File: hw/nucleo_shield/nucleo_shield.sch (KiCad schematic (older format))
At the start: 36 parts, among them CN101 Nucleo-F411RE-CN10, CN71 Nucleo-F411RE-CN7, P1 CONN_01X10, P2 CONN_01X10, P3 CONN_01X10, P4 CONN_01X02, P5 CONN_01X06, U1 74HC595, U2 74HC595, U3 LTV-847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

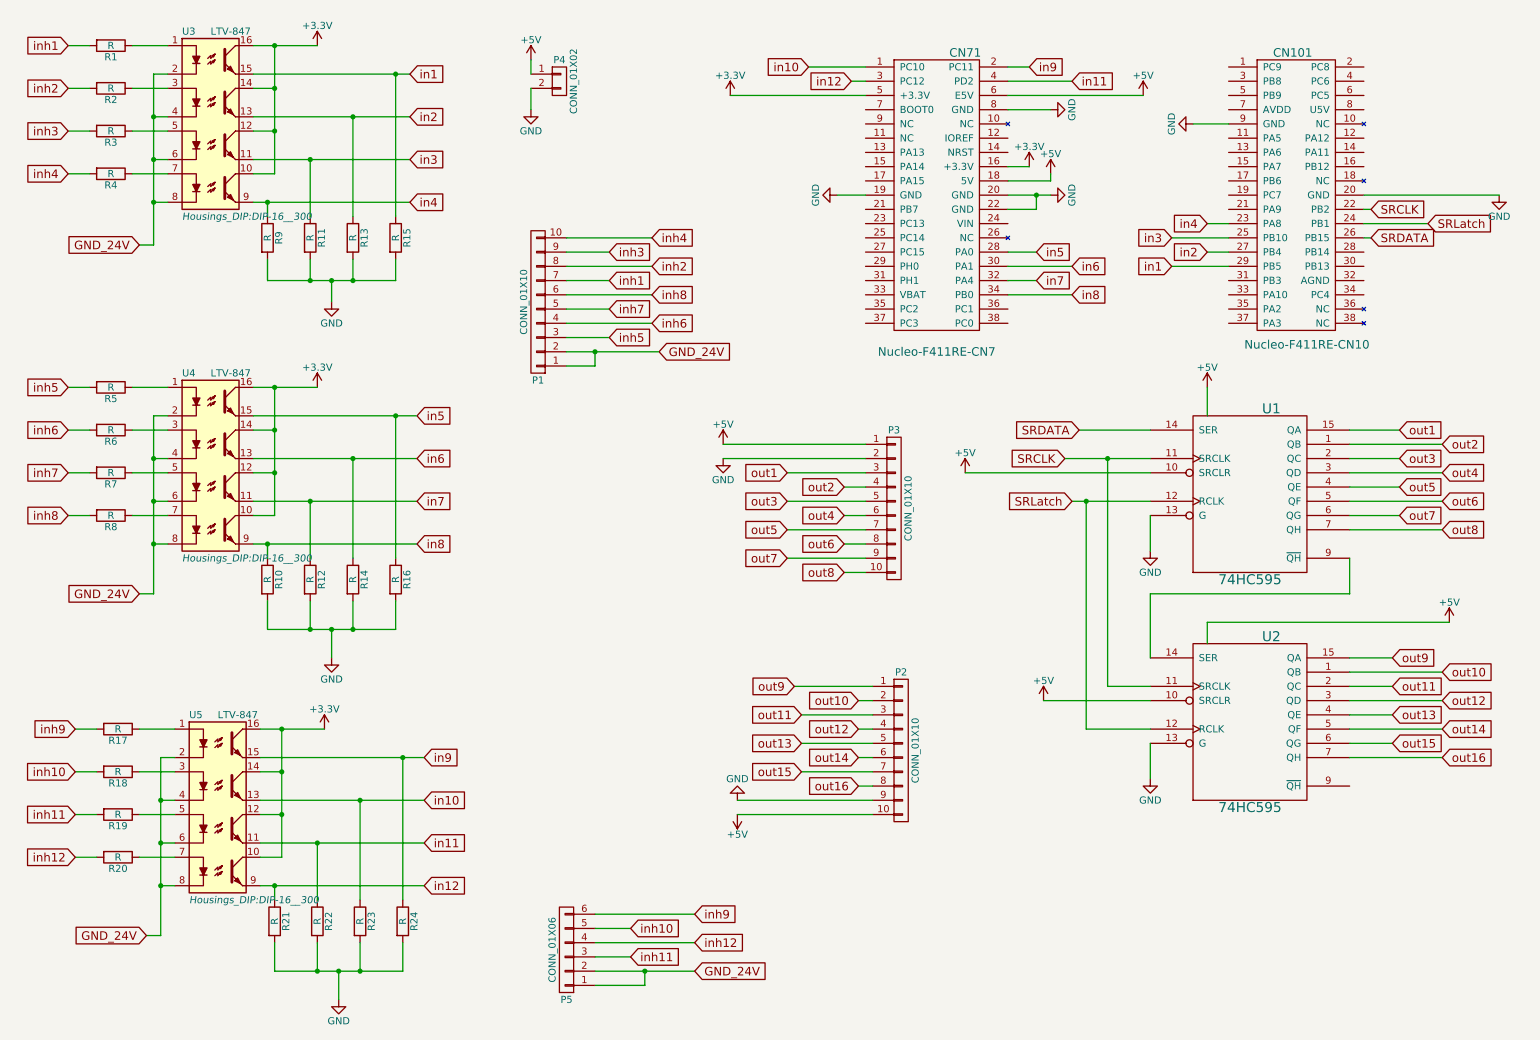
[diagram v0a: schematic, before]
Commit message: HW: modify nucleo with hierarchical sheets
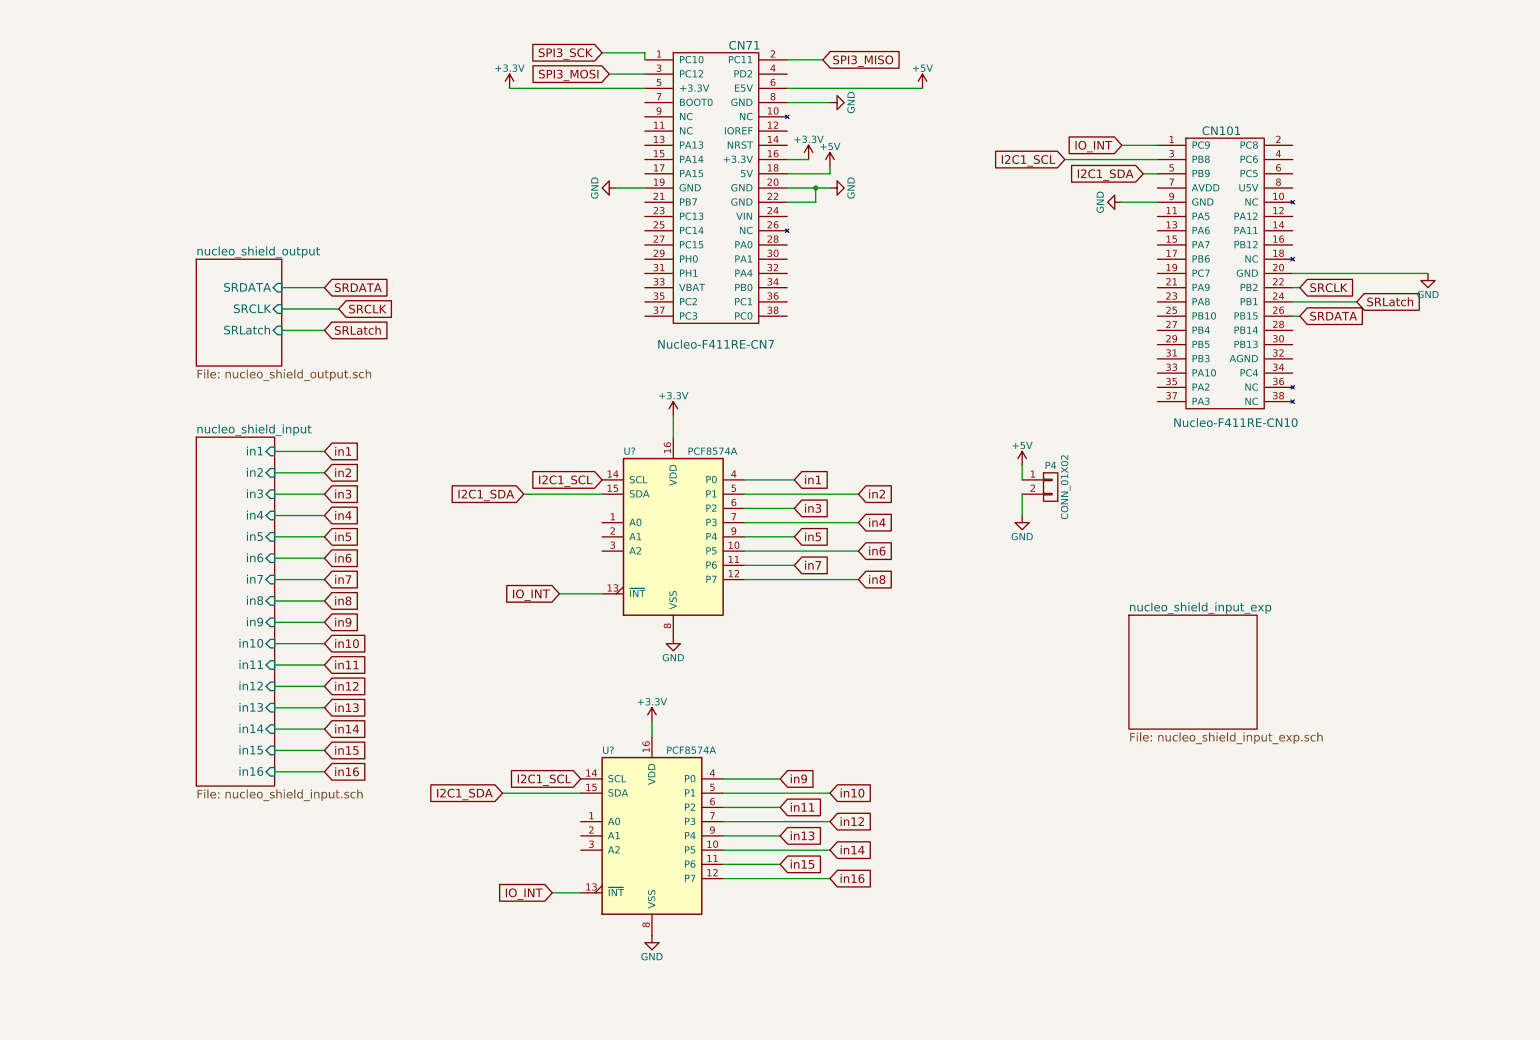
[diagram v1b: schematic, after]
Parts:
- removed P1, P2, P3: CONN_01X10, w_conn_screw:mors_10p, symbol CONN_01X10
- removed P5: CONN_01X06, w_conn_screw:mors_6p, symbol CONN_01X06
- removed R1, R10, R11, R12, R13, R14, R15, R16, R17, R18, R19, R2, R20, R21, R22, R23, R24, R3, R4, R5, R6, R7, R8, R9: R, Resistors_ThroughHole:Resistor_Horizontal_RM10mm, symbol R
- removed U1, U2: 74HC595, Housings_DIP:DIP-16__300, symbol 74HC595
- removed U3, U4, U5: LTV-847, Housings_DIP:DIP-16__300, symbol LTV-847
- added U? (x2): PCF8574A, symbol PCF8574A
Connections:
- net +3V3: now also U?.16 (VDD), U?.16 (VDD)
- net GND: now also U?.8 (VSS), U?.8 (VSS)
- net in1: now also U?.4 (P0); no longer CN101.29 (PB5)
- net in10: now also U?.5 (P1); no longer CN71.1 (PC10)
- net in11: now also U?.6 (P2); no longer CN71.4 (PD2)
- net in12: now also U?.7 (P3); no longer CN71.3 (PC12)
- net in2: now also U?.5 (P1); no longer CN101.27 (PB4)
- net in3: now also U?.6 (P2); no longer CN101.25 (PB10)
- net in4: now also U?.7 (P3); no longer CN101.23 (PA8)
- net in5: now also U?.9 (P4); no longer CN71.28 (PA0)
- net in6: now also U?.10 (P5); no longer CN71.30 (PA1)
- net in7: now also U?.11 (P6); no longer CN71.32 (PA4)
- net in8: now also U?.12 (P7); no longer CN71.34 (PB0)
- net in9: now also U?.4 (P0); no longer CN71.2 (PC11)
- net IO_INT: now reaches CN101.1 (PC9)
- net IO_INT: now also U?.13 (~INT~), U?.13 (~INT~)
- net I2C1_SCL: now reaches CN101.3 (PB8)
- net I2C1_SCL: now also U?.14 (SCL), U?.14 (SCL)
- net I2C1_SDA: now reaches CN101.5 (PB9)
- net I2C1_SDA: now also U?.15 (SDA), U?.15 (SDA)
- new net SPI3_MISO: CN71.2 (PC11)
- new net SPI3_MOSI: CN71.3 (PC12)
- new net SPI3_SCK: CN71.1 (PC10)
- new net in13: U?.9 (P4)
- new net in14: U?.10 (P5)
- new net in15: U?.11 (P6)
- new net in16: U?.12 (P7)
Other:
- moved on the sheet: CN101, CN71, P4

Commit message: Update schematic to add sct and io expander
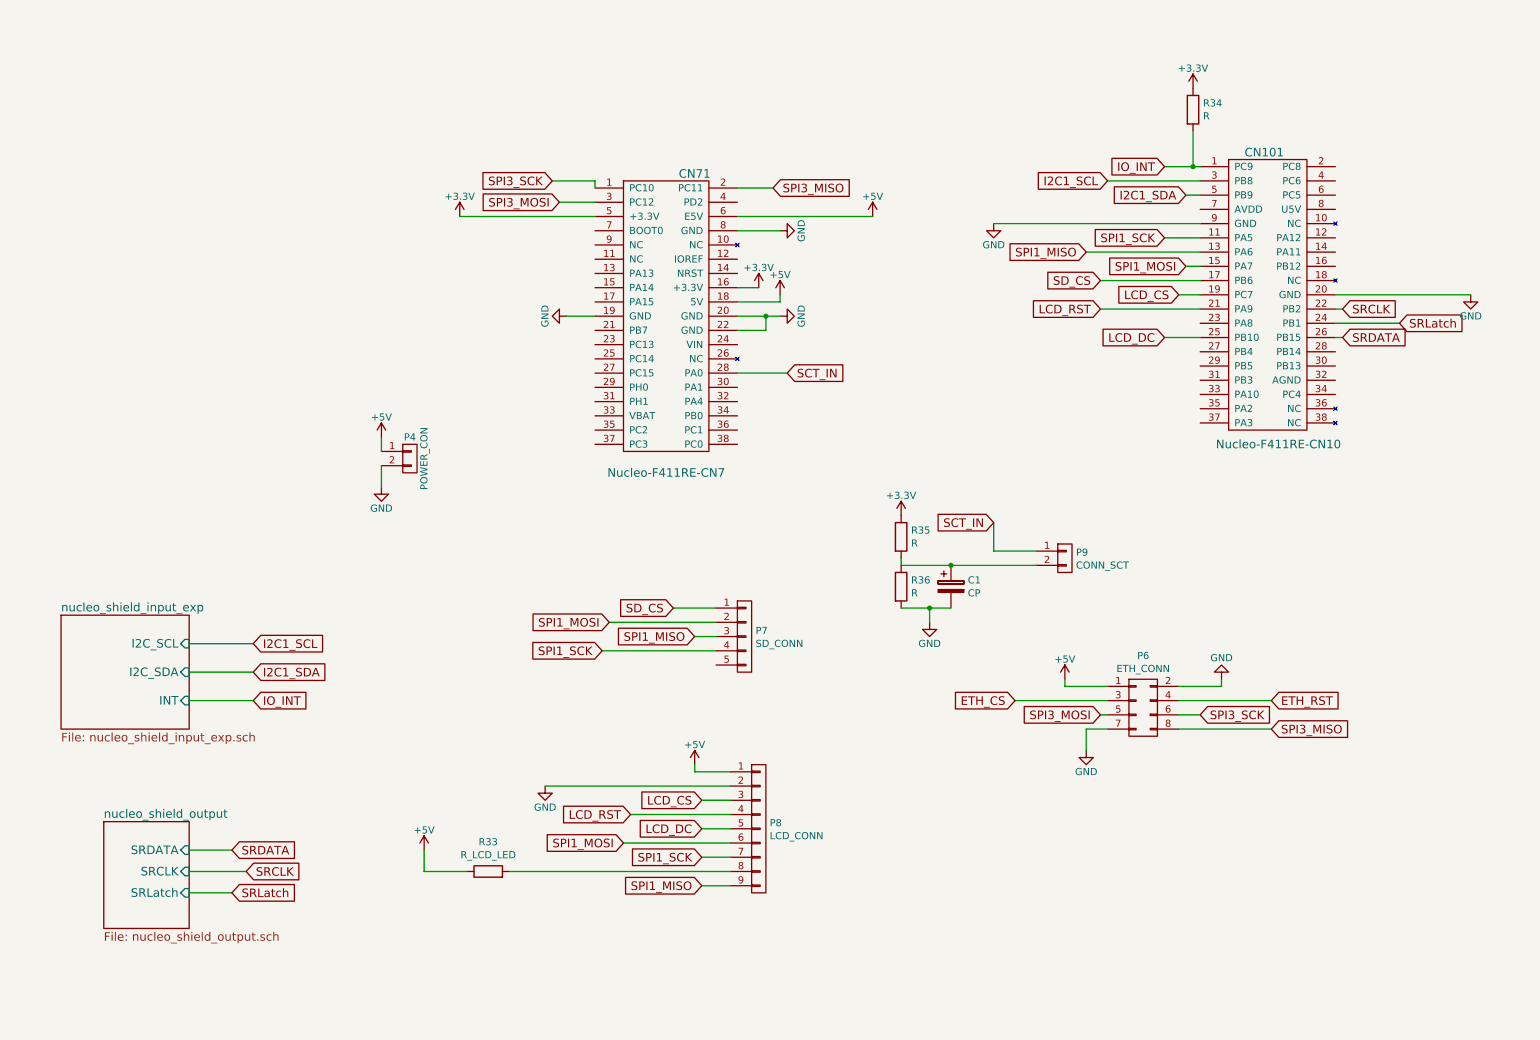
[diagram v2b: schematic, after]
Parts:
- removed U? (x2): PCF8574A, symbol PCF8574A
- added C1: CP, Capacitors_ThroughHole:C_Radial_D5_L11_P2, symbol CP
- added P6: ETH_CONN, Pin_Headers:Pin_Header_Straight_2x04, symbol CONN_02X04
- added P7: SD_CONN, Pin_Headers:Pin_Header_Straight_1x05, symbol CONN_01X05
- added P8: LCD_CONN, Pin_Headers:Pin_Header_Straight_1x09, symbol CONN_01X09
- added P9: CONN_SCT, Pin_Headers:Pin_Header_Straight_1x02, symbol CONN_01X02
- added R33: R_LCD_LED, Resistors_ThroughHole:Resistor_Horizontal_RM10mm, symbol R
- added R34, R35, R36: R, Resistors_ThroughHole:Resistor_Horizontal_RM10mm, symbol R
- P4: value CONN_01X02 -> POWER_CON
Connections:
- net +3V3: now also R34.1, R35.1
- net +5V: now also P6.1 (P1), P8.1 (P1), R33.1
- net GND: now also C1.2, P6.2 (P2), P6.7 (P7), P8.2 (P2), R36.2
- net IO_INT: now also R34.2
- net SPI3_MISO: now also P6.8 (P8)
- net SPI3_MOSI: now also P6.5 (P5)
- net SPI3_SCK: now also P6.6 (P6)
- net SPI1_SCK: now reaches CN101.11 (PA5)
- net SPI1_SCK: now also P7.4 (P4), P8.7 (P7)
- net SPI1_MISO: now reaches CN101.13 (PA6)
- net SPI1_MISO: now also P7.3 (P3), P8.9 (P9)
- net SPI1_MOSI: now reaches CN101.15 (PA7)
- net SPI1_MOSI: now also P7.2 (P2), P8.6 (P6)
- net SD_CS: now reaches CN101.17 (PB6)
- net SD_CS: now also P7.1 (P1)
- net LCD_CS: now reaches CN101.19 (PC7)
- net LCD_CS: now also P8.3 (P3)
- net LCD_RST: now reaches CN101.21 (PA9)
- net LCD_RST: now also P8.4 (P4)
- net LCD_DC: now reaches CN101.25 (PB10)
- net LCD_DC: now also P8.5 (P5)
- net SCT_IN: now reaches CN71.28 (PA0)
- net SCT_IN: now also P9.1 (P1)
- new net: P8.8 (P8), R33.2
- new net: C1.1, P9.2 (P2), R35.2, R36.1
- new net ETH_CS: P6.3 (P3)
- new net ETH_RST: P6.4 (P4)
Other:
- moved on the sheet: CN101, CN71, P4

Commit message: HW: fix a lot of connection and start positionning
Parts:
- removed R34: R, Resistors_ThroughHole:Resistor_Horizontal_RM10mm, symbol R
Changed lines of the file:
@@
 LIBS:memory
 LIBS:xilinx
-LIBS:special
 LIBS:microcontrollers
 LIBS:dsp
@@
 	4100 6600 5650 6600
 $Comp
-L +3.3V #PWR017
-U 1 1 572B08EB
-P 8900 1100
-F 0 "#PWR017" H 8900 950 50  0001 C CNN
-F 1 "+3.3V" H 8900 1240 50  0000 C CNN
-F 2 "" H 8900 1100 60  0000 C CNN
-F 3 "" H 8900 1100 60  0000 C CNN
-	1    8900 1100
-	1    0    0    -1
-$EndComp
-$Comp
-L R R34
-U 1 1 572B096D
-P 8900 1250
-F 0 "R34" H 8970 1296 50  0000 L CNN
-F 1 "R" H 8970 1205 50  0000 L CNN
-F 2 "Resistors_ThroughHole:Resistor_Horizontal_RM10mm" V 8830 1250 50  0001 C CNN
-F 3 "" H 8900 1250 50  0000 C CNN
-	1    8900 1250
-	1    0    0    -1
-$EndComp
-Wire Wire Line
-	8900 1650 8900 1400
-Connection ~ 8900 1650
-$Comp
-L +5V #PWR018
+L +5V #PWR017
 U 1 1 572B3B9C
 P 3500 6450
-F 0 "#PWR018" H 3500 6300 50  0001 C CNN
+F 0 "#PWR017" H 3500 6300 50  0001 C CNN
 F 1 "+5V" H 3500 6590 50  0000 C CNN
 F 2 "" H 3500 6450 60  0000 C CNN
@@
 SCT_IN
 $Comp
-L +3.3V #PWR019
+L +3.3V #PWR018
 U 1 1 572F3219
 P 6850 4100
-F 0 "#PWR019" H 6850 3950 50  0001 C CNN
+F 0 "#PWR018" H 6850 3950 50  0001 C CNN
 F 1 "+3.3V" H 6850 4240 50  0000 C CNN
 F 2 "" H 6850 4100 60  0000 C CNN
@@
 $EndComp
 $Comp
-L GND #PWR020
+L GND #PWR019
 U 1 1 572F337B
 P 7050 4850
-F 0 "#PWR020" H 7050 4600 50  0001 C CNN
+F 0 "#PWR019" H 7050 4600 50  0001 C CNN
 F 1 "GND" H 7050 4700 50  0000 C CNN
 F 2 "" H 7050 4850 60  0000 C CNN
